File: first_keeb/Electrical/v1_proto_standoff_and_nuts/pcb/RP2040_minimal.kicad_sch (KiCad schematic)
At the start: 75 parts, among them J1 Conn_01x04_Socket, J2 Conn_01x04_Socket, P1 USB-TYPE-C-016, Q1 SN74LV1T34DBV, SW1 SKRKAHE020, SW2 SKRKAHE020, SW3 BUTT1, SW4 BUTT3, SW5 BUTT2, SW6 MS-22C01-G010, SW7 SK-3296S-01-L3, SW8 MS-22C01-G010, U1 AMS1117-2.5, U2 ME6208A44M3G, U3 PRTR5V0U2X, U4 STM32F401RCTx, U5 MCP6001-OT, U6 MCP6001-OT, Y1 16MHz

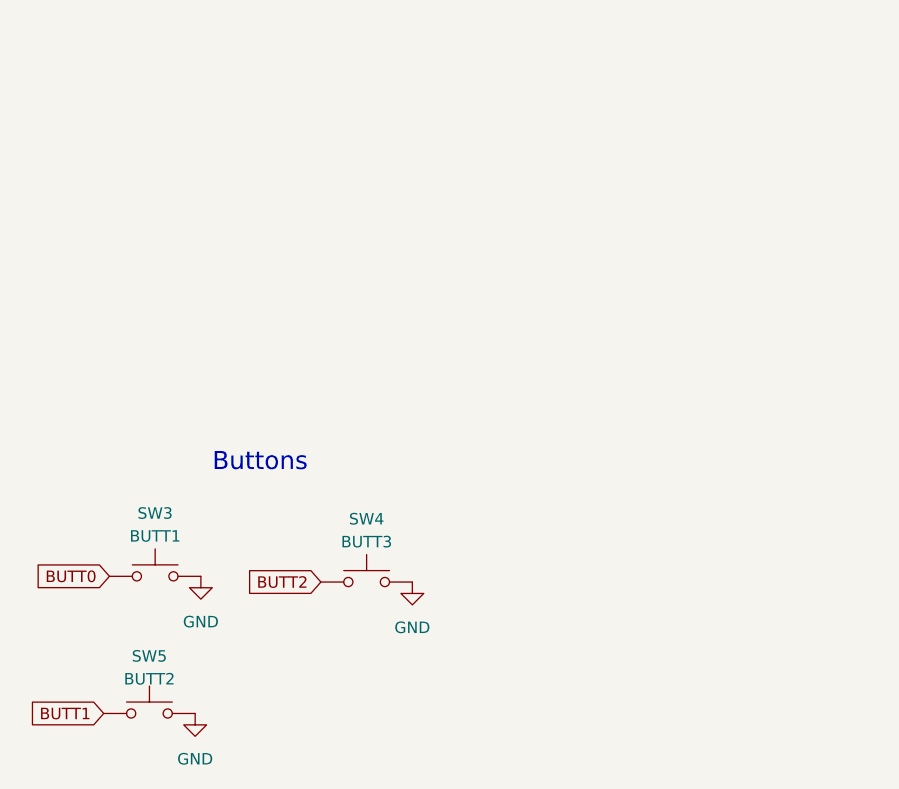
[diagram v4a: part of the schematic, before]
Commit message: generate prod files for pcb
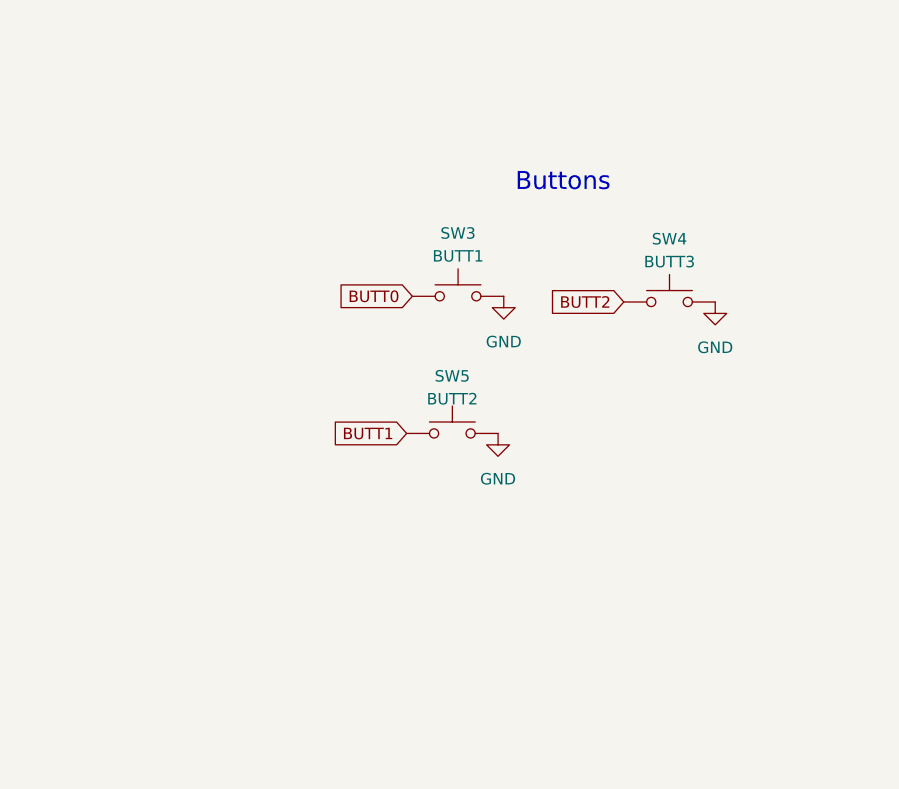
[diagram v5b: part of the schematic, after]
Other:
- moved on the sheet: SW3, SW4, SW5
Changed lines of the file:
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@@
     (effects (font (size 2.54 2.54)) (justify left bottom))
   )
-  (text "Buttons" (at 33.02 247.65 0)
+  (text "Buttons" (at 66.675 216.535 0)
     (effects (font (size 2 2)) (justify left bottom))
   )
@@
     )
   )
-  (global_label "BUTT2" (shape input) (at 45.085 259.715 180) (fields_autoplaced)
+  (global_label "BUTT2" (shape input) (at 78.74 228.6 180) (fields_autoplaced)
     (effects (font (size 1.27 1.27)) (justify right))
-    (property "Intersheetrefs" "${INTERSHEET_REFS}" (at 37.0882 259.715 0)
+    (property "Intersheetrefs" "${INTERSHEET_REFS}" (at 70.7432 228.6 0)
       (effects (font (size 1.27 1.27)) (justify right) hide)
     )
@@
     )
   )
-  (global_label "BUTT1" (shape input) (at 20.955 274.32 180) (fields_autoplaced)
+  (global_label "BUTT1" (shape input) (at 54.61 243.205 180) (fields_autoplaced)
     (effects (font (size 1.27 1.27)) (justify right))
-    (property "Intersheetrefs" "${INTERSHEET_REFS}" (at 12.9582 274.32 0)
+    (property "Intersheetrefs" "${INTERSHEET_REFS}" (at 46.6132 243.205 0)
       (effects (font (size 1.27 1.27)) (justify right) hide)
     )
@@
     )
   )
-  (global_label "BUTT0" (shape input) (at 21.59 259.08 180) (fields_autoplaced)
+  (global_label "BUTT0" (shape input) (at 55.245 227.965 180) (fields_autoplaced)
     (effects (font (size 1.27 1.27)) (justify right))
-    (property "Intersheetrefs" "${INTERSHEET_REFS}" (at 13.5932 259.08 0)
+    (property "Intersheetrefs" "${INTERSHEET_REFS}" (at 47.2482 227.965 0)
       (effects (font (size 1.27 1.27)) (justify right) hide)
     )
@@
     )
   )
-  (symbol (lib_name "GND_1") (lib_id "power:GND") (at 31.75 259.08 0) (unit 1)
+  (symbol (lib_name "GND_1") (lib_id "power:GND") (at 65.405 227.965 0) (unit 1)
     (in_bom yes) (on_board yes) (dnp no) (fields_autoplaced)
-    (property "Reference" "#PWR074" (at 31.75 265.43 0)
+    (property "Reference" "#PWR074" (at 65.405 234.315 0)
       (effects (font (size 1.27 1.27)) hide)
     )
-    (property "Value" "GND" (at 31.75 264.16 0)
+    (property "Value" "GND" (at 65.405 233.045 0)
       (effects (font (size 1.27 1.27)))
     )
-    (property "Footprint" "" (at 31.75 259.08 0)
+    (property "Footprint" "" (at 65.405 227.965 0)
       (effects (font (size 1.27 1.27)) hide)
     )
-    (property "Datasheet" "" (at 31.75 259.08 0)
+    (property "Datasheet" "" (at 65.405 227.965 0)
       (effects (font (size 1.27 1.27)) hide)
     )
@@
     )
   )
-  (symbol (lib_name "GND_1") (lib_id "power:GND") (at 31.115 274.32 0) (unit 1)
+  (symbol (lib_name "GND_1") (lib_id "power:GND") (at 64.77 243.205 0) (unit 1)
     (in_bom yes) (on_board yes) (dnp no) (fields_autoplaced)
-    (property "Reference" "#PWR079" (at 31.115 280.67 0)
+    (property "Reference" "#PWR079" (at 64.77 249.555 0)
       (effects (font (size 1.27 1.27)) hide)
     )
-    (property "Value" "GND" (at 31.115 279.4 0)
+    (property "Value" "GND" (at 64.77 248.285 0)
       (effects (font (size 1.27 1.27)))
     )
-    (property "Footprint" "" (at 31.115 274.32 0)
+    (property "Footprint" "" (at 64.77 243.205 0)
       (effects (font (size 1.27 1.27)) hide)
     )
-    (property "Datasheet" "" (at 31.115 274.32 0)
+    (property "Datasheet" "" (at 64.77 243.205 0)
       (effects (font (size 1.27 1.27)) hide)
     )
@@
     )
   )
-  (symbol (lib_id "Switch:SW_Push") (at 26.035 274.32 0) (unit 1)
+  (symbol (lib_id "Switch:SW_Push") (at 59.69 243.205 0) (unit 1)
     (in_bom yes) (on_board yes) (dnp no) (fields_autoplaced)
-    (property "Reference" "SW5" (at 26.035 267.97 0)
+    (property "Reference" "SW5" (at 59.69 236.855 0)
       (effects (font (size 1.27 1.27)))
     )
-    (property "Value" "BUTT2" (at 26.035 270.51 0)
+    (property "Value" "BUTT2" (at 59.69 239.395 0)
       (effects (font (size 1.27 1.27)))
     )
-    (property "Footprint" "Button_Switch_SMD:SW_Push_1P1T_NO_6x6mm_H9.5mm" (at 26.035 269.24 0)
+    (property "Footprint" "Button_Switch_SMD:SW_Push_1P1T_NO_6x6mm_H9.5mm" (at 59.69 238.125 0)
       (effects (font (size 1.27 1.27)) hide)
     )
-    (property "Datasheet" "~" (at 26.035 269.24 0)
+    (property "Datasheet" "~" (at 59.69 238.125 0)
       (effects (font (size 1.27 1.27)) hide)
     )
@@
     )
   )
-  (symbol (lib_id "Switch:SW_Push") (at 50.165 259.715 0) (unit 1)
+  (symbol (lib_id "Switch:SW_Push") (at 83.82 228.6 0) (unit 1)
     (in_bom yes) (on_board yes) (dnp no) (fields_autoplaced)
-    (property "Reference" "SW4" (at 50.165 252.73 0)
+    (property "Reference" "SW4" (at 83.82 221.615 0)
       (effects (font (size 1.27 1.27)))
     )
-    (property "Value" "BUTT3" (at 50.165 255.27 0)
+    (property "Value" "BUTT3" (at 83.82 224.155 0)
       (effects (font (size 1.27 1.27)))
     )
-    (property "Footprint" "Button_Switch_SMD:SW_Push_1P1T_NO_6x6mm_H9.5mm" (at 50.165 254.635 0)
+    (property "Footprint" "Button_Switch_SMD:SW_Push_1P1T_NO_6x6mm_H9.5mm" (at 83.82 223.52 0)
       (effects (font (size 1.27 1.27)) hide)
     )
-    (property "Datasheet" "~" (at 50.165 254.635 0)
+    (property "Datasheet" "~" (at 83.82 223.52 0)
       (effects (font (size 1.27 1.27)) hide)
     )
@@
     )
   )
-  (symbol (lib_id "Switch:SW_Push") (at 26.67 259.08 0) (unit 1)
+  (symbol (lib_id "Switch:SW_Push") (at 60.325 227.965 0) (unit 1)
     (in_bom yes) (on_board yes) (dnp no) (fields_autoplaced)
-    (property "Reference" "SW3" (at 26.67 252.095 0)
+    (property "Reference" "SW3" (at 60.325 220.98 0)
       (effects (font (size 1.27 1.27)))
     )
-    (property "Value" "BUTT1" (at 26.67 254.635 0)
+    (property "Value" "BUTT1" (at 60.325 223.52 0)
       (effects (font (size 1.27 1.27)))
     )
-    (property "Footprint" "Button_Switch_SMD:SW_Push_1P1T_NO_6x6mm_H9.5mm" (at 26.67 254 0)
+    (property "Footprint" "Button_Switch_SMD:SW_Push_1P1T_NO_6x6mm_H9.5mm" (at 60.325 222.885 0)
       (effects (font (size 1.27 1.27)) hide)
     )
-    (property "Datasheet" "~" (at 26.67 254 0)
+    (property "Datasheet" "~" (at 60.325 222.885 0)
       (effects (font (size 1.27 1.27)) hide)
     )
@@
     )
   )
-  (symbol (lib_name "GND_1") (lib_id "power:GND") (at 55.245 259.715 0) (unit 1)
+  (symbol (lib_name "GND_1") (lib_id "power:GND") (at 88.9 228.6 0) (unit 1)
     (in_bom yes) (on_board yes) (dnp no) (fields_autoplaced)
-    (property "Reference" "#PWR075" (at 55.245 266.065 0)
+    (property "Reference" "#PWR075" (at 88.9 234.95 0)
       (effects (font (size 1.27 1.27)) hide)
     )
-    (property "Value" "GND" (at 55.245 264.795 0)
+    (property "Value" "GND" (at 88.9 233.68 0)
       (effects (font (size 1.27 1.27)))
     )
-    (property "Footprint" "" (at 55.245 259.715 0)
+    (property "Footprint" "" (at 88.9 228.6 0)
       (effects (font (size 1.27 1.27)) hide)
     )
-    (property "Datasheet" "" (at 55.245 259.715 0)
+    (property "Datasheet" "" (at 88.9 228.6 0)
       (effects (font (size 1.27 1.27)) hide)
     )

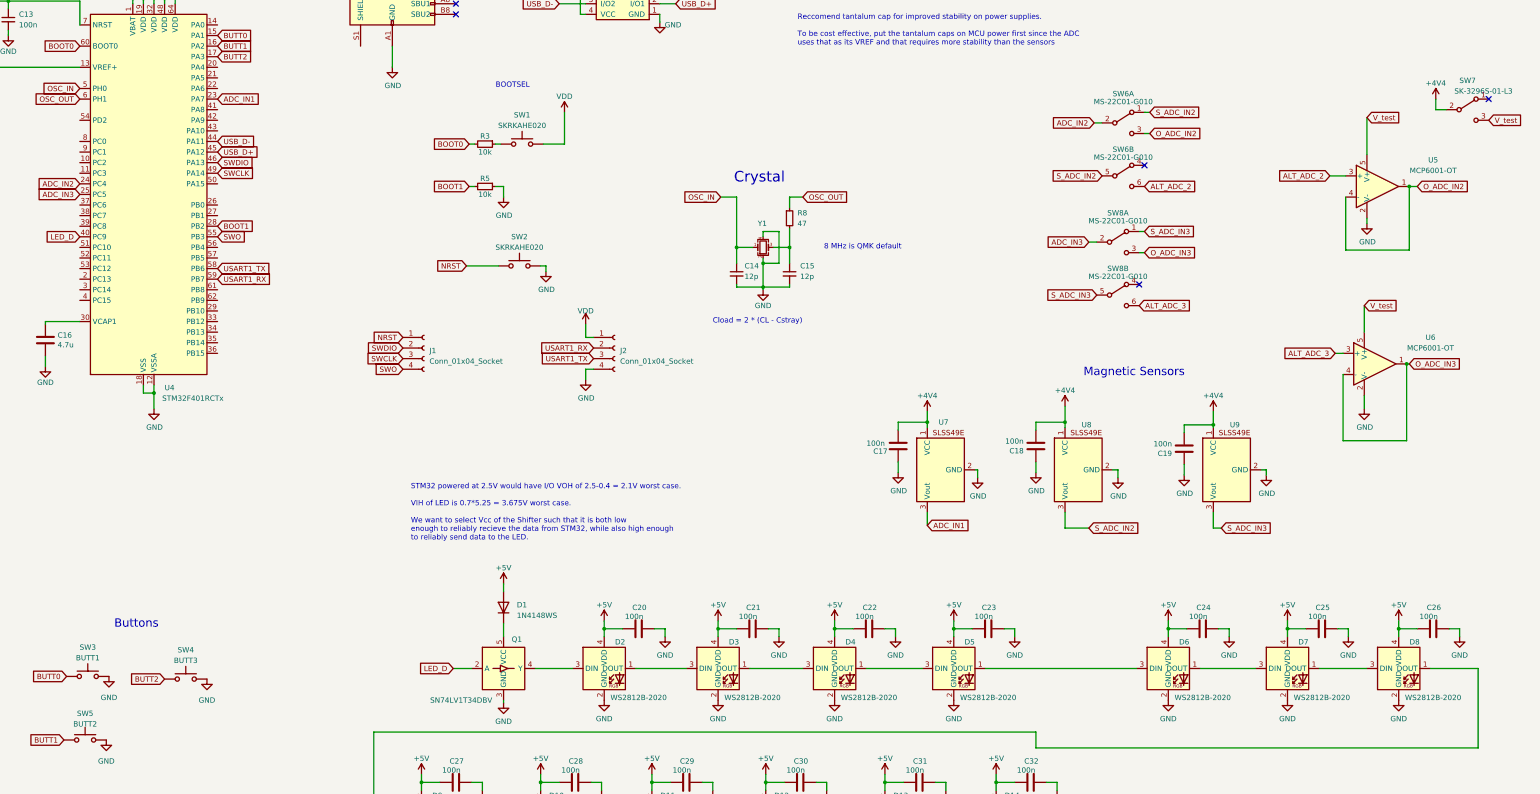
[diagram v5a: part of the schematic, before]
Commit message: fixes lcsc number in bom
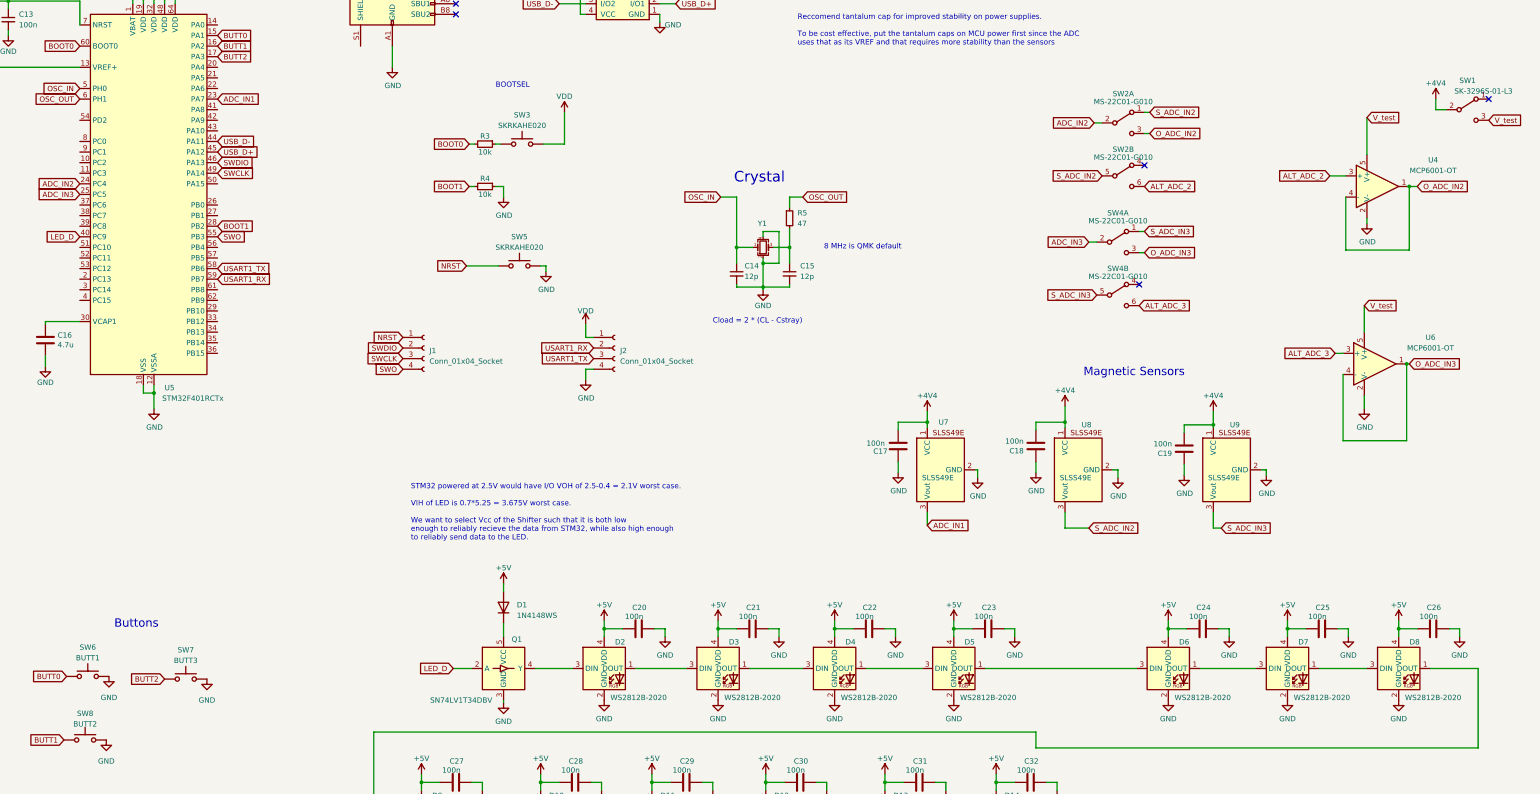
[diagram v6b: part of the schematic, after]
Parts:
- C13: LCSC Part # C19666 -> C1525
- U7, U8, U9: value ~ -> SLSS49E
- Y1: value 16MHz -> 8MHz
- renumbered R5 to R4, R8 to R5, SW7 to SW1, SW6 to SW2, SW1 to SW3, SW8 to SW4, SW2 to SW5, SW3 to SW6, SW4 to SW7, SW5 to SW8, U5 to U4, U4 to U5

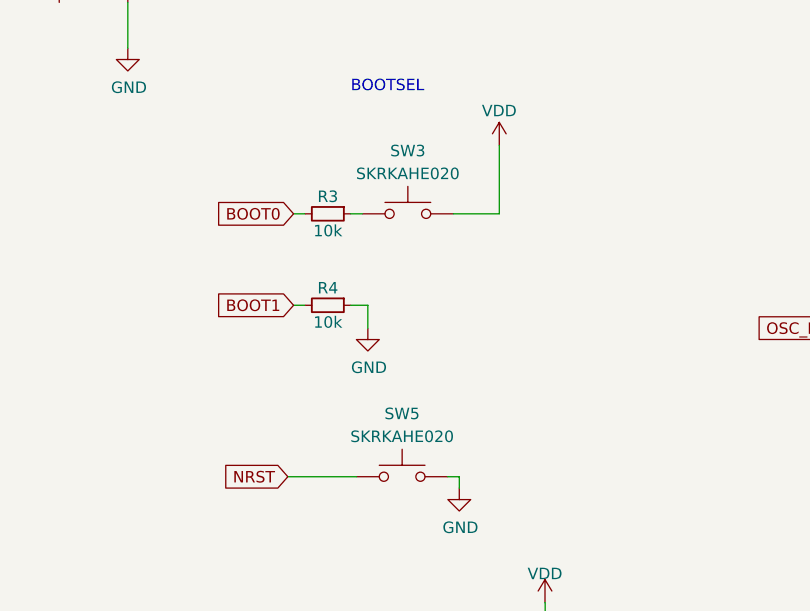
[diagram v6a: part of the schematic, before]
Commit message: adds  basic part switch
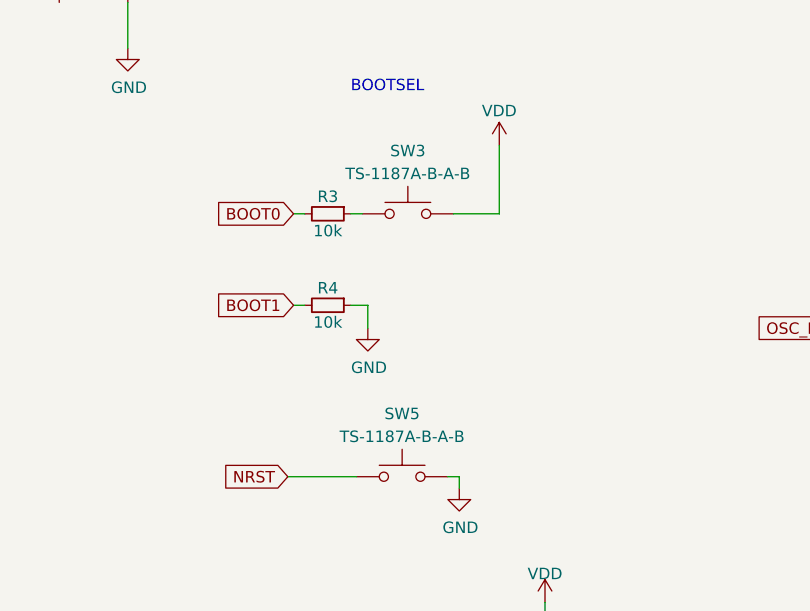
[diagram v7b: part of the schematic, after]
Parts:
- SW3, SW5: value SKRKAHE020 -> TS-1187A-B-A-B; footprint Button_Switch_SMD:SW_Push_SPST_NO_Alps_SKRK -> Button_Switch_SMD:TS-1187A
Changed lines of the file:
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@@
       (effects (font (size 1.27 1.27)))
     )
-    (property "Value" "SKRKAHE020" (at 163.83 125.095 0)
+    (property "Value" "TS-1187A-B-A-B" (at 163.83 125.095 0)
       (effects (font (size 1.27 1.27)))
     )
-    (property "Footprint" "Button_Switch_SMD:SW_Push_SPST_NO_Alps_SKRK" (at 163.83 124.46 0)
+    (property "Footprint" "Button_Switch_SMD:TS-1187A" (at 163.83 124.46 0)
       (effects (font (size 1.27 1.27)) hide)
     )
@@
       (effects (font (size 1.27 1.27)))
     )
-    (property "Value" "SKRKAHE020" (at 164.465 95.885 0)
+    (property "Value" "TS-1187A-B-A-B" (at 164.465 95.885 0)
       (effects (font (size 1.27 1.27)))
     )
-    (property "Footprint" "Button_Switch_SMD:SW_Push_SPST_NO_Alps_SKRK" (at 164.465 95.25 0)
+    (property "Footprint" "Button_Switch_SMD:TS-1187A" (at 164.465 95.25 0)
       (effects (font (size 1.27 1.27)) hide)
     )
